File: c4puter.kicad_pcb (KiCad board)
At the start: 6 copper layers, 200 x 200 mm, 207 parts, among them J1 PDI, J2 MICROSD, J7 19V 3A, J8 DEBUG, Q1 AOD4189, Q2 AOD4189, Q3 2N7002, U1 ATXMEGA8E5-MU

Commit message: workworkwork
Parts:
- removed REF**: MP, MP
- added C57: 22u, IPC7351-Nominal:CAPC2012X70, F.Cu at (48.8, 161.5)
- added C59: C-0402, IPC7351-Nominal:CAPC1005X55, F.Cu at (48.8, 164.2)
- added C75: 22u, IPC7351-Nominal:CAPC2012X70, F.Cu at (57.5, 162.8)
- added C76: 22u, IPC7351-Nominal:CAPC2012X70, F.Cu at (55.2, 162.8)
- added L2: 2u2, manuf:BOURNS-SRN3015, F.Cu at (52.0, 157.8)
- added MP1: SCREW, mech:SCREW-4-SUPPORTED, F.Cu at (119.0, 104.0)
- added MP2: SCREW, mech:SCREW-4-SUPPORTED, F.Cu at (77.0, 130.0)
- added MP3: SCREW, mech:SCREW-4-SUPPORTED, F.Cu at (33.0, 104.0)
- added MP4: SCREW, mech:SCREW-4-SUPPORTED, F.Cu at (92.0, 32.0)
- added Q5: BSH203, smd-semi:SOT-23, F.Cu at (56.5, 159.0)
- added R57: R-0402, IPC7351-Nominal:RESC1005X40, F.Cu at (51.5, 165.8)
- added R61: R-0402, IPC7351-Nominal:RESC1005X40, F.Cu at (48.8, 165.8)
- added R62: 100, IPC7351-Nominal:RESC1608X50, F.Cu at (56.5, 156.2)
- added U2: AS7C38098A, IPC7351-Nominal:SOP80P1176X120-44, F.Cu at (61.0, 133.0)
- added U3: AS7C38098A, IPC7351-Nominal:SOP80P1176X120-44, F.Cu at (93.0, 133.0)
- added U5: AP3429A, smd-semi:SOT-23-5, F.Cu at (52.0, 162.5)
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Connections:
- net /PerBus/PCI_AD00 renamed /PCI/AD0
- net /PerBus/PCI_AD02 renamed /PCI/AD2
- net /PerBus/PCI_AD03 renamed /PCI/AD3
- net /PerBus/PCI_AD04 renamed /PCI/AD4
- net /PerBus/PCI_AD05 renamed /PCI/AD5
- net /PerBus/PCI_AD06 renamed /PCI/AD6
- net /PerBus/PCI_AD07 renamed /PCI/AD7
- net /PerBus/PCI_AD08 renamed /PCI/AD8
- net /PerBus/PCI_AD09 renamed /PCI/AD9
- net /PerBus/PCI_AD10 renamed /PCI/AD10
- net /PerBus/PCI_AD11 renamed /PCI/AD11
- net /PerBus/PCI_AD12 renamed /PCI/AD12
- net /PerBus/PCI_AD13 renamed /PCI/AD13
- net /PerBus/PCI_AD14 renamed /PCI/AD14
- net /PerBus/PCI_AD15 renamed /PCI/AD15
- net /PerBus/PCI_AD16 renamed /PCI/AD16
- net /PerBus/PCI_AD17 renamed /PCI/AD17
- net /PerBus/PCI_AD18 renamed /PCI/AD18
- net /PerBus/PCI_AD19 renamed /PCI/AD19
- net /PerBus/PCI_AD20 renamed /PCI/AD20
- net /PerBus/PCI_AD21 renamed /PCI/AD21
- net /PerBus/PCI_AD22 renamed /PCI/AD22
- net /PerBus/PCI_AD23 renamed /PCI/AD23
- net /PerBus/PCI_AD24 renamed /PCI/AD24
- net /PerBus/PCI_AD25 renamed /PCI/AD25
- net /PerBus/PCI_AD26 renamed /PCI/AD26
- net /PerBus/PCI_AD27 renamed /PCI/AD27
- net /PerBus/PCI_AD28 renamed /PCI/AD28
- net /PerBus/PCI_AD29 renamed /PCI/AD29
- net /PerBus/PCI_AD30 renamed /PCI/AD30
- net /PerBus/PCI_AD31 renamed /PCI/AD31
- net /PerBus/PCI_CBE#0 renamed /PCI/~CBE0
- net /PerBus/PCI_CBE#1 renamed /PCI/~CBE1
- net /PerBus/PCI_CBE#2 renamed /PCI/~CBE2
- net /PerBus/PCI_CBE#3 renamed /PCI/~CBE3
- net /PerBus/PCI_CLK renamed /PCI/CLK
- net /PerBus/PCI_DEVSEL# renamed /PCI/~DEVSEL
- net /PerBus/PCI_FRAME# renamed /PCI/~FRAME
- net /PerBus/PCI_GNT#0 renamed /PCI/~GNT0
- net /PerBus/PCI_GNT#1 renamed /PCI/~GNT1
- net /PerBus/PCI_GNT#2 renamed /PCI/~GNT2
- net /PerBus/PCI_GNT#3 renamed /PCI/~GNT3
- net /PerBus/PCI_IDSEL0 renamed /PCI/IDSEL0
- net /PerBus/PCI_IDSEL1 renamed /PCI/IDSEL1
- net /PerBus/PCI_IDSEL2 renamed /PCI/IDSEL2
- net /PerBus/PCI_IDSEL3 renamed /PCI/IDSEL3
- net /PerBus/PCI_INTA# renamed /PCI/~INT0
- net /PerBus/PCI_INTB# renamed /PCI/~INT1
- net /PerBus/PCI_INTC# renamed /PCI/~INT2
- net /PerBus/PCI_INTD# renamed /PCI/~INT3
- net /PerBus/PCI_IRDY# renamed /PCI/~IRDY
- net /PerBus/PCI_LOCK# renamed /PCI/~LOCK
- net /PerBus/PCI_M66EN renamed /PCI/M66EN
- net /PerBus/PCI_N12 renamed N12_PCI
- net /PerBus/PCI_P12 renamed P12_PCI
- net /PerBus/PCI_P5 renamed P5_PCI
- net /PerBus/PCI_PAR renamed /PCI/PAR
- net /PerBus/PCI_PERR# renamed /Multibridge/~PCI_PERR
- net /PerBus/PCI_PRSNT1#0 renamed /PCI/~PRSNT1_0
- net /PerBus/PCI_PRSNT1#1 renamed /PCI/~PRSNT1_1
- net /PerBus/PCI_PRSNT1#2 renamed /PCI/~PRSNT1_2
- net /PerBus/PCI_PRSNT1#3 renamed /PCI/~PRSNT1_3
- net /PerBus/PCI_PRSNT2#0 renamed /PCI/~PRSNT2_0
- net /PerBus/PCI_PRSNT2#1 renamed /PCI/~PRSNT2_1
- net /PerBus/PCI_PRSNT2#2 renamed /PCI/~PRSNT2_2
- net /PerBus/PCI_PRSNT2#3 renamed /PCI/~PRSNT2_3
- net /PerBus/PCI_REQ#0 renamed /Multibridge/~PCI_REQ0
- net /PerBus/PCI_REQ#1 renamed /Multibridge/~PCI_REQ1
- net /PerBus/PCI_REQ#2 renamed /Multibridge/~PCI_REQ2
- net /PerBus/PCI_REQ#3 renamed /Multibridge/~PCI_REQ3
- net /PerBus/PCI_RST# renamed /PCI/~RST
- net /PerBus/PCI_SERR# renamed /Multibridge/~PCI_SERR
- net /PerBus/PCI_SMBCLK renamed /PCI/SCL
- net /PerBus/PCI_SMBDAT renamed /PCI/SDA
- net /PerBus/PCI_STOP# renamed /Multibridge/~PCI_STOP
- net /PerBus/PCI_TCK renamed /PCI/PCI_TCK
- net /PerBus/PCI_TDI renamed /PCI/PCI_TDI
- net /PerBus/PCI_TDO renamed /PCI/PCI_TDO
- net /PerBus/PCI_TMS renamed /PCI/PCI_TMS
- net /PerBus/PCI_TRDY# renamed /Multibridge/~PCI_TRDY
- net /PerBus/PCI_TRST# renamed /PCI/PCI_TRST#
- net Net-(BRIDGE1-PadC12) renamed /Multibridge/SDRAMCLK
- net Net-(BRIDGE1-PadM20) renamed /Multibridge/PCICLK
- net VCCAUX renamed P3V3_BRIDGE
- net VCORE renamed P1V2_BRIDGE
- BRIDGE1 pad AB12: /PerBus/PCI_PME# -> Net-(BRIDGE1-PadAB12)
- BRIDGE1 pad T19: Net-(BRIDGE1-PadT19) -> /Multibridge/DQ63
- BRIDGE1 pad T20: /Multibridge/DQ63 -> Net-(BRIDGE1-PadT20)
- BRIDGE1 pad Y4: /PerBus/PCI_AD01 -> /PCI/AD1
- C37 pad 1: /PerBus/PCI_VIO -> P3V3_PCI
- C38 pad 1: /PerBus/PCI_P3V3 -> P3V3_PCI
- C41 pad 1: /PerBus/PCI_VIO -> P3V3_PCI
- C42 pad 1: /PerBus/PCI_P3V3 -> P3V3_PCI
- C45 pad 1: /PerBus/PCI_VIO -> P3V3_PCI
- C46 pad 1: /PerBus/PCI_P3V3 -> P3V3_PCI
- C49 pad 1: /PerBus/PCI_VIO -> P3V3_PCI
- C50 pad 1: /PerBus/PCI_P3V3 -> P3V3_PCI
- CPU0 pad A1: (no net) -> GND
- CPU0 pad A10: Net-(CPU0-PadA10) -> (no net)
- CPU0 pad A11: Net-(CPU0-PadA11) -> (no net)
- CPU0 pad A12: Net-(CPU0-PadA12) -> (no net)
- CPU0 pad A13: Net-(CPU0-PadA13) -> (no net)
- CPU0 pad A14: Net-(CPU0-PadA14) -> (no net)
- CPU0 pad A15: Net-(CPU0-PadA15) -> (no net)
- CPU0 pad A16: Net-(CPU0-PadA16) -> (no net)
- CPU0 pad A17: Net-(CPU0-PadA17) -> (no net)
- CPU0 pad A18: Net-(CPU0-PadA18) -> (no net)
- CPU0 pad A19: (no net) -> /Power Distrib/CPU0_TDO
- CPU0 pad A22: (no net) -> GND
- CPU0 pad A3: Net-(CPU0-PadA3) -> (no net)
- CPU0 pad A4: Net-(CPU0-PadA4) -> (no net)
- CPU0 pad A5: Net-(CPU0-PadA5) -> (no net)
- CPU0 pad A6: Net-(CPU0-PadA6) -> (no net)
- CPU0 pad A7: Net-(CPU0-PadA7) -> (no net)
- CPU0 pad A8: Net-(CPU0-PadA8) -> (no net)
- CPU0 pad A9: Net-(CPU0-PadA9) -> (no net)
- CPU0 pad AA1: (no net) -> Net-(CPU0-PadAA1)
- CPU0 pad AA10: (no net) -> Net-(CPU0-PadAA10)
- CPU0 pad AA11: (no net) -> P3V3_CPU
- CPU0 pad AA12: (no net) -> Net-(CPU0-PadAA12)
- CPU0 pad AA13: (no net) -> GND
- CPU0 pad AA14: (no net) -> Net-(CPU0-PadAA14)
- CPU0 pad AA15: (no net) -> P3V3_CPU
- CPU0 pad AA16: (no net) -> Net-(CPU0-PadAA16)
- CPU0 pad AA17: (no net) -> GND
- CPU0 pad AA18: (no net) -> Net-(CPU0-PadAA18)
- CPU0 pad AA19: (no net) -> P3V3_CPU
- CPU0 pad AA2: (no net) -> Net-(CPU0-PadAA2)
- CPU0 pad AA20: (no net) -> Net-(CPU0-PadAA20)
- CPU0 pad AA21: (no net) -> Net-(CPU0-PadAA21)
- CPU0 pad AA22: (no net) -> Net-(CPU0-PadAA22)
- CPU0 pad AA3: (no net) -> P3V3_CPU
- CPU0 pad AA4: (no net) -> Net-(CPU0-PadAA4)
- CPU0 pad AA5: (no net) -> GND
- CPU0 pad AA6: (no net) -> Net-(CPU0-PadAA6)
- CPU0 pad AA7: (no net) -> P3V3_CPU
- CPU0 pad AA8: (no net) -> Net-(CPU0-PadAA8)
- CPU0 pad AA9: (no net) -> GND
- CPU0 pad AB1: (no net) -> GND
- CPU0 pad AB10: (no net) -> Net-(CPU0-PadAB10)
- CPU0 pad AB11: (no net) -> Net-(CPU0-PadAB11)
- CPU0 pad AB12: (no net) -> Net-(CPU0-PadAB12)
- CPU0 pad AB13: (no net) -> Net-(CPU0-PadAB13)
- CPU0 pad AB14: (no net) -> Net-(CPU0-PadAB14)
- CPU0 pad AB15: (no net) -> Net-(CPU0-PadAB15)
- CPU0 pad AB16: (no net) -> Net-(CPU0-PadAB16)
- CPU0 pad AB17: (no net) -> Net-(CPU0-PadAB17)
- CPU0 pad AB18: (no net) -> Net-(CPU0-PadAB18)
- CPU0 pad AB19: (no net) -> Net-(CPU0-PadAB19)
- CPU0 pad AB2: (no net) -> Net-(CPU0-PadAB2)
- CPU0 pad AB20: (no net) -> Net-(CPU0-PadAB20)
- CPU0 pad AB21: (no net) -> Net-(CPU0-PadAB21)
- CPU0 pad AB22: (no net) -> GND
- CPU0 pad AB3: (no net) -> Net-(CPU0-PadAB3)
- CPU0 pad AB4: (no net) -> Net-(CPU0-PadAB4)
- CPU0 pad AB5: (no net) -> Net-(CPU0-PadAB5)
- CPU0 pad AB6: (no net) -> Net-(CPU0-PadAB6)
- CPU0 pad AB7: (no net) -> Net-(CPU0-PadAB7)
- CPU0 pad AB8: (no net) -> Net-(CPU0-PadAB8)
- CPU0 pad AB9: (no net) -> Net-(CPU0-PadAB9)
- CPU0 pad B10: Net-(CPU0-PadB10) -> (no net)
- CPU0 pad B11: Net-(CPU0-PadB11) -> (no net)
- CPU0 pad B12: Net-(CPU0-PadB12) -> (no net)
- CPU0 pad B13: (no net) -> GND
- CPU0 pad B14: Net-(CPU0-PadB14) -> (no net)
- CPU0 pad B15: Net-(CPU0-PadB15) -> (no net)
- CPU0 pad B16: Net-(CPU0-PadB16) -> (no net)
- CPU0 pad B17: (no net) -> GND
- CPU0 pad B18: Net-(CPU0-PadB18) -> (no net)
- CPU0 pad B19: Net-(CPU0-PadB19) -> (no net)
- CPU0 pad B4: Net-(CPU0-PadB4) -> (no net)
- CPU0 pad B5: (no net) -> GND
- CPU0 pad B6: Net-(CPU0-PadB6) -> (no net)
- CPU0 pad B7: Net-(CPU0-PadB7) -> (no net)
- CPU0 pad B8: Net-(CPU0-PadB8) -> (no net)
- CPU0 pad B9: (no net) -> GND
- CPU0 pad C10: Net-(CPU0-PadC10) -> (no net)
- CPU0 pad C11: Net-(CPU0-PadC11) -> (no net)
- CPU0 pad C12: Net-(CPU0-PadC12) -> (no net)
- CPU0 pad C13: Net-(CPU0-PadC13) -> (no net)
- CPU0 pad C14: Net-(CPU0-PadC14) -> (no net)
- CPU0 pad C15: Net-(CPU0-PadC15) -> (no net)
- CPU0 pad C16: Net-(CPU0-PadC16) -> (no net)
- CPU0 pad C17: Net-(CPU0-PadC17) -> (no net)
- CPU0 pad C18: (no net) -> /Power Distrib/CPU0_TMS
- CPU0 pad C5: Net-(CPU0-PadC5) -> (no net)
- CPU0 pad C6: Net-(CPU0-PadC6) -> (no net)
- CPU0 pad C7: Net-(CPU0-PadC7) -> (no net)
- CPU0 pad C8: Net-(CPU0-PadC8) -> (no net)
- CPU0 pad C9: Net-(CPU0-PadC9) -> (no net)
- CPU0 pad D10: Net-(CPU0-PadD10) -> (no net)
- CPU0 pad D11: Net-(CPU0-PadD11) -> (no net)
- CPU0 pad D12: Net-(CPU0-PadD12) -> (no net)
- CPU0 pad D13: Net-(CPU0-PadD13) -> (no net)
- CPU0 pad D14: Net-(CPU0-PadD14) -> (no net)
- CPU0 pad D15: Net-(CPU0-PadD15) -> (no net)
- CPU0 pad D16: (no net) -> P3V3_CPU
- CPU0 pad D17: Net-(CPU0-PadD17) -> (no net)
- CPU0 pad D18: (no net) -> GND
- CPU0 pad D4: (no net) -> GND
- CPU0 pad D6: Net-(CPU0-PadD6) -> (no net)
- CPU0 pad D7: Net-(CPU0-PadD7) -> (no net)
- CPU0 pad D8: Net-(CPU0-PadD8) -> (no net)
- CPU0 pad D9: Net-(CPU0-PadD9) -> (no net)
- CPU0 pad E11: (no net) -> GND
- CPU0 pad E12: Net-(CPU0-PadE12) -> (no net)
- CPU0 pad E13: Net-(CPU0-PadE13) -> (no net)
- CPU0 pad E14: Net-(CPU0-PadE14) -> (no net)
- CPU0 pad E15: (no net) -> GND
- CPU0 pad E16: Net-(CPU0-PadE16) -> (no net)
- CPU0 pad E17: Net-(CPU0-PadE17) -> (no net)
- CPU0 pad E18: (no net) -> /Power Distrib/CPU0_TDI
- CPU0 pad E2: (no net) -> GND
- CPU0 pad E21: (no net) -> GND
- CPU0 pad E7: (no net) -> GND
- CPU0 pad E9: Net-(CPU0-PadE9) -> (no net)
- CPU0 pad F11: (no net) -> P3V3_CPU
- CPU0 pad F12: Net-(CPU0-PadF12) -> (no net)
- CPU0 pad F13: Net-(CPU0-PadF13) -> (no net)
- CPU0 pad F14: Net-(CPU0-PadF14) -> (no net)
- CPU0 pad F15: Net-(CPU0-PadF15) -> (no net)
- CPU0 pad G10: Net-(CPU0-PadG10) -> (no net)
- CPU0 pad G12: (no net) -> P3V3_CPU
- CPU0 pad G13: Net-(CPU0-PadG13) -> (no net)
- CPU0 pad G14: Net-(CPU0-PadG14) -> (no net)
- CPU0 pad G15: (no net) -> /Power Distrib/CPU0_TCK
- CPU0 pad G18: (no net) -> GND
- CPU0 pad G5: (no net) -> GND
- CPU0 pad H12: Net-(CPU0-PadH12) -> (no net)
- CPU0 pad H13: Net-(CPU0-PadH13) -> (no net)
- CPU0 pad H14: Net-(CPU0-PadH14) -> (no net)
- CPU0 pad H15: (no net) -> P3V3_CPU
- CPU0 pad H7: (no net) -> GND
- CPU0 pad H9: (no net) -> P3V3_CPU
- CPU0 pad J10: (no net) -> P1V2_CPU
- CPU0 pad J11: (no net) -> GND
- CPU0 pad J12: (no net) -> P1V2_CPU
- CPU0 pad J13: (no net) -> GND
- CPU0 pad J14: (no net) -> P1V2_CPU
- CPU0 pad J15: (no net) -> GND
- CPU0 pad J2: (no net) -> GND
- CPU0 pad J21: (no net) -> GND
- CPU0 pad J8: (no net) -> P1V2_CPU
- CPU0 pad J9: (no net) -> GND
- CPU0 pad K10: (no net) -> GND
- CPU0 pad K11: (no net) -> P1V2_CPU
- CPU0 pad K12: (no net) -> GND
- CPU0 pad K13: (no net) -> P1V2_CPU
- CPU0 pad K14: (no net) -> GND
- CPU0 pad K15: (no net) -> P3V3_CPU
- CPU0 pad K9: (no net) -> P1V2_CPU
- CPU0 pad L10: (no net) -> P1V2_CPU
- CPU0 pad L11: (no net) -> GND
- CPU0 pad L12: (no net) -> P1V2_CPU
- CPU0 pad L13: (no net) -> GND
- CPU0 pad L14: (no net) -> P1V2_CPU
- CPU0 pad L18: (no net) -> GND
- CPU0 pad L5: (no net) -> GND
- CPU0 pad L8: (no net) -> P3V3_CPU
- CPU0 pad L9: (no net) -> GND
- CPU0 pad M10: (no net) -> GND
- CPU0 pad M11: (no net) -> P1V2_CPU
- CPU0 pad M12: (no net) -> GND
- CPU0 pad M13: (no net) -> P1V2_CPU
- CPU0 pad M14: (no net) -> GND
- CPU0 pad M15: (no net) -> P3V3_CPU
- CPU0 pad M9: (no net) -> P1V2_CPU
- CPU0 pad N10: (no net) -> P1V2_CPU
- CPU0 pad N11: (no net) -> GND
- CPU0 pad N12: (no net) -> P1V2_CPU
- CPU0 pad N13: (no net) -> GND
- CPU0 pad N14: (no net) -> P1V2_CPU
- CPU0 pad N15: (no net) -> /Power Distrib/CPU0_SUSP
- CPU0 pad N17: (no net) -> GND
- CPU0 pad N2: (no net) -> GND
- CPU0 pad N21: (no net) -> GND
- CPU0 pad N8: (no net) -> P3V3_CPU
- CPU0 pad N9: (no net) -> GND
- CPU0 pad P10: (no net) -> GND
- CPU0 pad P11: (no net) -> P1V2_CPU
- CPU0 pad P12: (no net) -> GND
- CPU0 pad P13: (no net) -> P1V2_CPU
- CPU0 pad P14: (no net) -> GND
- CPU0 pad P9: (no net) -> P1V2_CPU
- CPU0 pad R10: (no net) -> P3V3_CPU
- CPU0 pad R11: (no net) -> Net-(CPU0-PadR11)
- CPU0 pad R12: (no net) -> P3V3_CPU
- CPU0 pad R14: (no net) -> P1V2_CPU
- CPU0 pad R18: (no net) -> GND
- CPU0 pad R5: (no net) -> GND
- CPU0 pad R6: (no net) -> P3V3_CPU
- CPU0 pad R7: (no net) -> Net-(CPU0-PadR7)
- CPU0 pad R8: (no net) -> Net-(CPU0-PadR8)
- CPU0 pad R9: (no net) -> Net-(CPU0-PadR9)
- CPU0 pad T11: (no net) -> Net-(CPU0-PadT11)
- CPU0 pad T13: (no net) -> P3V3_CPU
- CPU0 pad T5: (no net) -> Net-(CPU0-PadT5)
- CPU0 pad T6: (no net) -> Net-(CPU0-PadT6)
- CPU0 pad T7: (no net) -> Net-(CPU0-PadT7)
- CPU0 pad T9: (no net) -> P3V3_CPU
- CPU0 pad U11: (no net) -> P3V3_CPU
- CPU0 pad U13: (no net) -> Net-(CPU0-PadU13)
- CPU0 pad U14: (no net) -> Net-(CPU0-PadU14)
- CPU0 pad U15: (no net) -> Net-(CPU0-PadU15)
- CPU0 pad U2: (no net) -> GND
- CPU0 pad U21: (no net) -> GND
- CPU0 pad U6: (no net) -> Net-(CPU0-PadU6)
- CPU0 pad U7: (no net) -> GND
- CPU0 pad U9: (no net) -> Net-(CPU0-PadU9)
- CPU0 pad V10: (no net) -> GND
- CPU0 pad V11: (no net) -> Net-(CPU0-PadV11)
- CPU0 pad V12: (no net) -> P3V3_CPU
- CPU0 pad V13: (no net) -> Net-(CPU0-PadV13)
- CPU0 pad V14: (no net) -> GND
- CPU0 pad V15: (no net) -> Net-(CPU0-PadV15)
- CPU0 pad V16: (no net) -> P3V3_CPU
- CPU0 pad V4: (no net) -> GND
- CPU0 pad V5: (no net) -> Net-(CPU0-PadV5)
- CPU0 pad V6: (no net) -> P3V3_CPU
- CPU0 pad V7: (no net) -> Net-(CPU0-PadV7)
- CPU0 pad V8: (no net) -> P3V3_CPU
- CPU0 pad V9: (no net) -> Net-(CPU0-PadV9)
- CPU0 pad W10: (no net) -> Net-(CPU0-PadW10)
- CPU0 pad W11: (no net) -> Net-(CPU0-PadW11)
- CPU0 pad W12: (no net) -> Net-(CPU0-PadW12)
- CPU0 pad W13: (no net) -> Net-(CPU0-PadW13)
- CPU0 pad W14: (no net) -> Net-(CPU0-PadW14)
- CPU0 pad W15: (no net) -> Net-(CPU0-PadW15)
- CPU0 pad W16: (no net) -> GND
- CPU0 pad W18: (no net) -> Net-(CPU0-PadW18)
- CPU0 pad W19: (no net) -> GND
- CPU0 pad W4: (no net) -> Net-(CPU0-PadW4)
- CPU0 pad W5: (no net) -> P3V3_CPU
- CPU0 pad W6: (no net) -> Net-(CPU0-PadW6)
- CPU0 pad W7: (no net) -> GND
- CPU0 pad W8: (no net) -> Net-(CPU0-PadW8)
- CPU0 pad W9: (no net) -> Net-(CPU0-PadW9)
- CPU0 pad Y10: (no net) -> Net-(CPU0-PadY10)
- CPU0 pad Y11: (no net) -> Net-(CPU0-PadY11)
- CPU0 pad Y12: (no net) -> Net-(CPU0-PadY12)
- CPU0 pad Y13: (no net) -> Net-(CPU0-PadY13)
- CPU0 pad Y14: (no net) -> Net-(CPU0-PadY14)
- CPU0 pad Y15: (no net) -> Net-(CPU0-PadY15)
- CPU0 pad Y16: (no net) -> Net-(CPU0-PadY16)
- CPU0 pad Y17: (no net) -> Net-(CPU0-PadY17)
- CPU0 pad Y18: (no net) -> Net-(CPU0-PadY18)
- CPU0 pad Y19: (no net) -> Net-(CPU0-PadY19)
- CPU0 pad Y20: (no net) -> Net-(CPU0-PadY20)
- CPU0 pad Y21: (no net) -> Net-(CPU0-PadY21)
- CPU0 pad Y22: (no net) -> Net-(CPU0-PadY22)
- CPU0 pad Y3: (no net) -> Net-(CPU0-PadY3)
- CPU0 pad Y4: (no net) -> Net-(CPU0-PadY4)
- CPU0 pad Y5: (no net) -> Net-(CPU0-PadY5)
- CPU0 pad Y6: (no net) -> Net-(CPU0-PadY6)
- CPU0 pad Y7: (no net) -> Net-(CPU0-PadY7)
- CPU0 pad Y8: (no net) -> Net-(CPU0-PadY8)
- CPU0 pad Y9: (no net) -> Net-(CPU0-PadY9)
- CPU1 pad A1: (no net) -> GND
- CPU1 pad A19: (no net) -> /Power Distrib/CPU1_TDO
- CPU1 pad A22: (no net) -> GND
- CPU1 pad AA13: (no net) -> GND
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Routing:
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- added copper zone on B.Cu, net P3V3_PCI
- removed copper zone on B.Cu, net /PerBus/PCI_P3V3
- removed copper zone on B.Cu, net /PerBus/PCI_VIO
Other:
- net class Default: clearance 0.125 -> 0.1016; trace_width 0.125 -> 0.1016
- rule trace_clearance: 0.125 -> 0.1016

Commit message: workworkworkwork
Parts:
- removed C57, C75, C76: 22u, IPC7351-Nominal:CAPC2012X70
- removed C59: C-0402, IPC7351-Nominal:CAPC1005X55
- removed L2: 2u2, manuf:BOURNS-SRN3015
- removed Q5: BSH203, smd-semi:SOT-23
- removed R57, R61: R-0402, IPC7351-Nominal:RESC1005X40
- removed R62: 100, IPC7351-Nominal:RESC1608X50
- removed U5: AP3429A, smd-semi:SOT-23-5

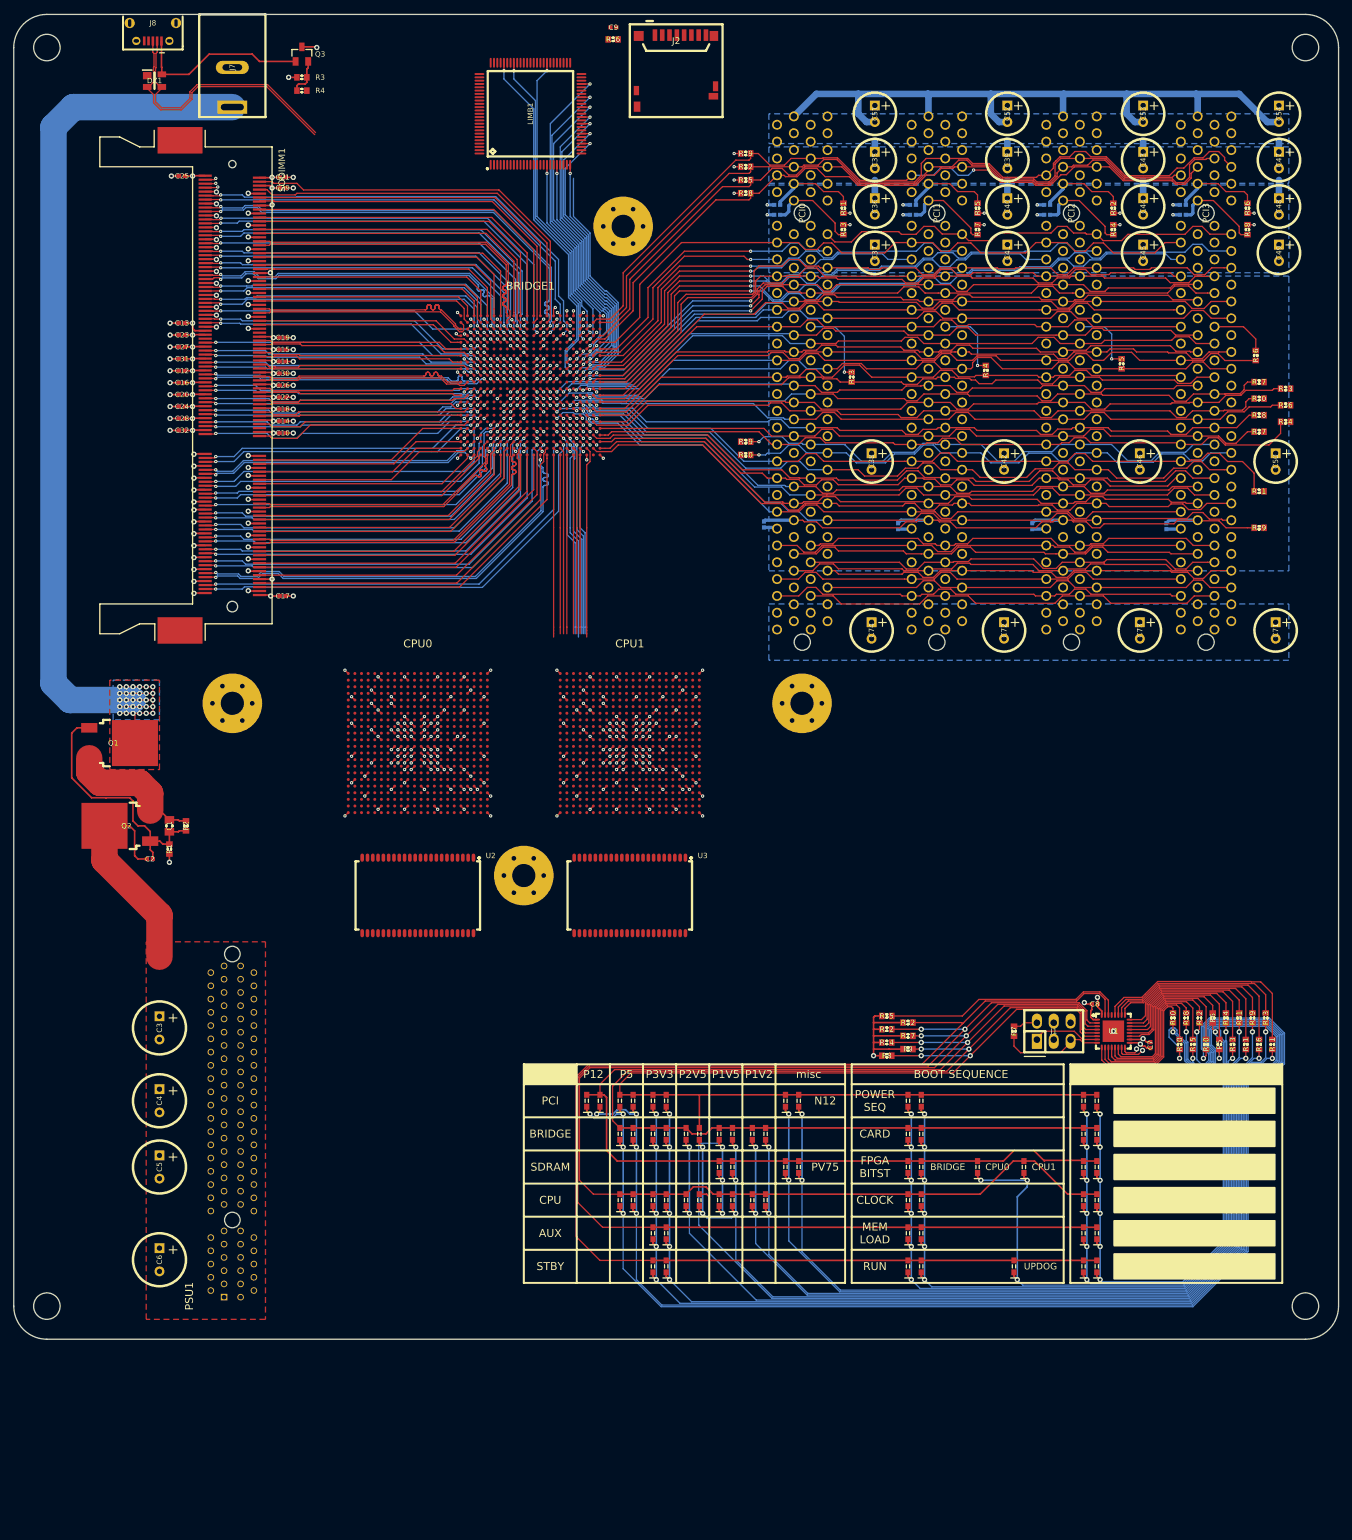
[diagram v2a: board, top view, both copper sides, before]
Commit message: Route CPU bus and cache
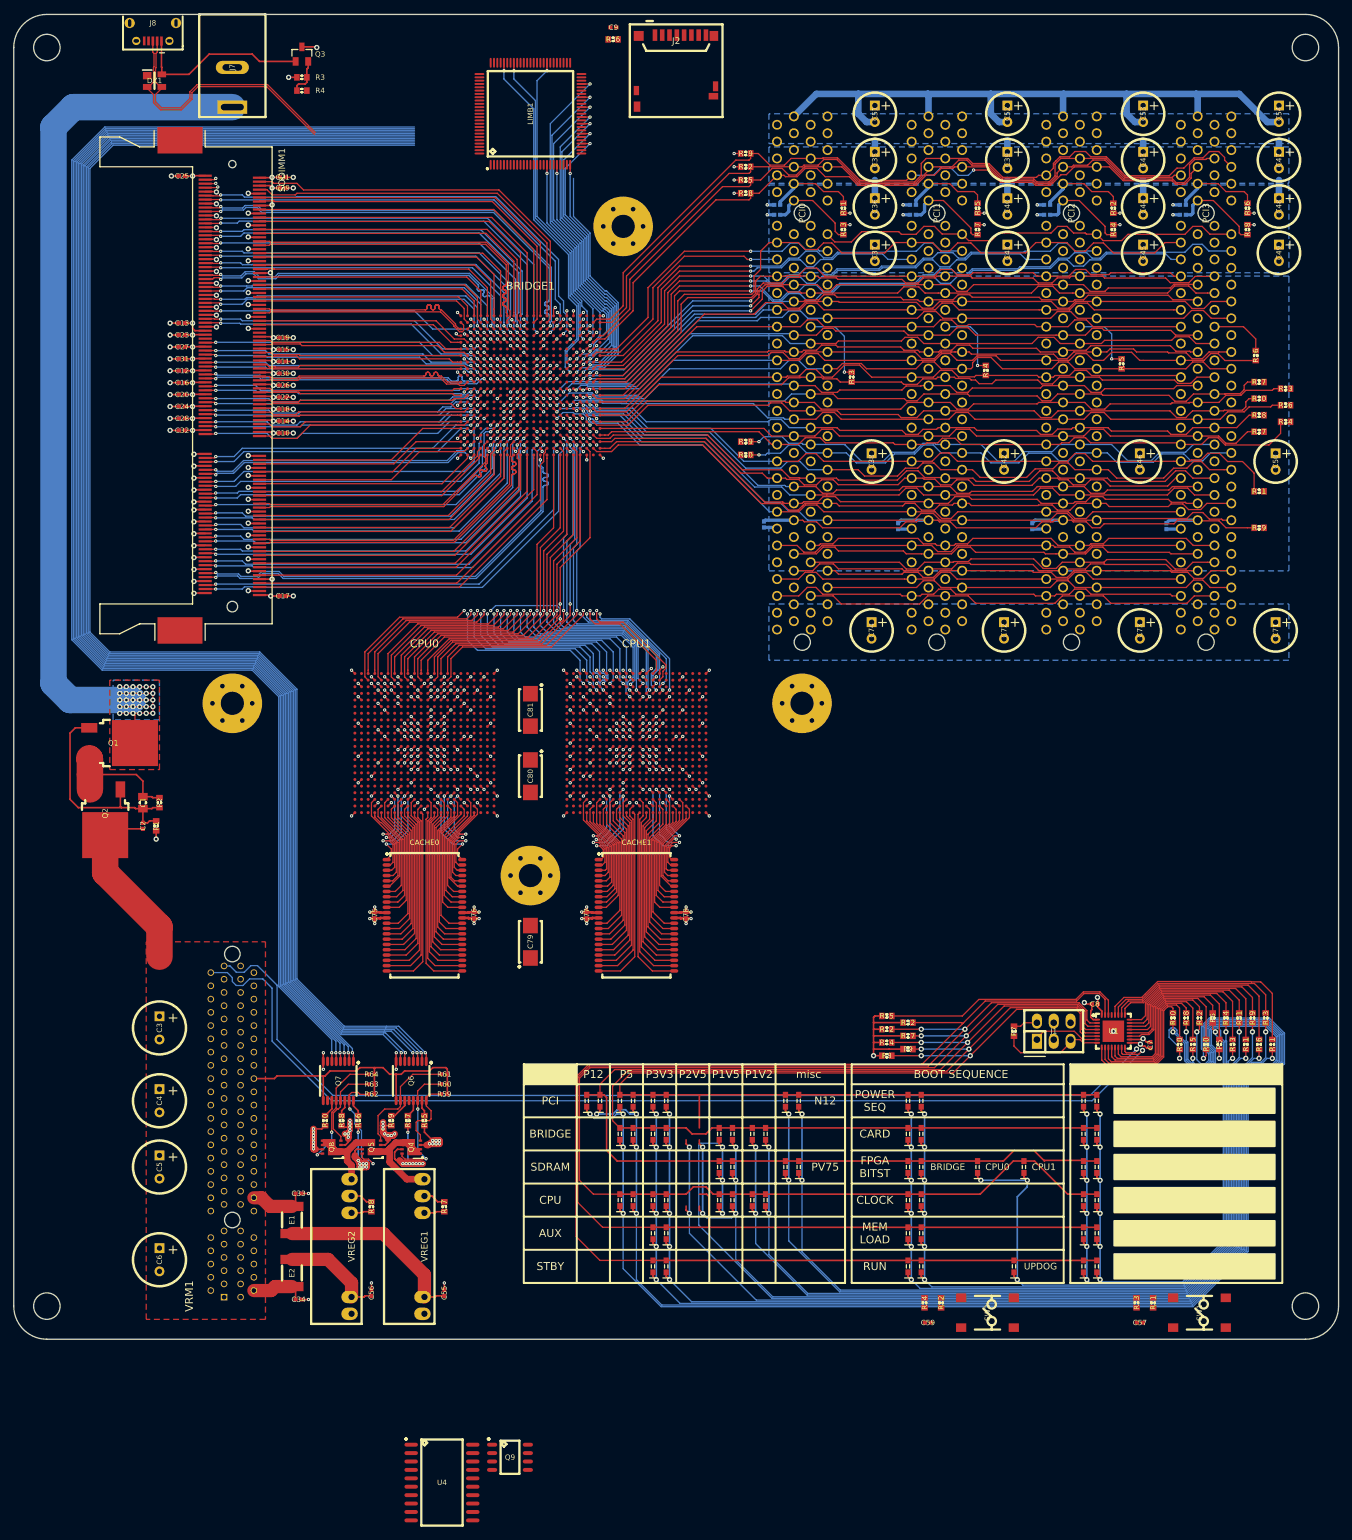
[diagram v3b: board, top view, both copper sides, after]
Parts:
- removed DS19: BRG_P2V5(R), smd-semi:LED-0603
- removed DS20: CPU_P2V5(R), smd-semi:LED-0603
- removed DS21: BRG_P2V5(G), smd-semi:LED-0603
- removed DS22: CPU_P2V5(G), smd-semi:LED-0603
- added C33: 100n, IPC7351-Nominal:CAPC1005X55, F.Cu at (43.0, 178.0)
- added C34: 100n, IPC7351-Nominal:CAPC1005X55, F.Cu at (43.0, 194.0)
- added C55: 100n, IPC7351-Nominal:CAPC1005X55, F.Cu at (65.0, 193.0)
- added C56: 100n, IPC7351-Nominal:CAPC1005X55, F.Cu at (54.0, 193.0)
- added C57: 100n, IPC7351-Nominal:CAPC1005X55, F.Cu at (170.0, 197.5)
- added C59: 100n, IPC7351-Nominal:CAPC1005X55, F.Cu at (138.0, 197.5)
- added C75: 1u, IPC7351-Nominal:CAPC1005X55, F.Cu at (54.5, 136.0)
- added C76: 1u, IPC7351-Nominal:CAPC1005X55, F.Cu at (69.5, 136.0)
- added C77: 1u, IPC7351-Nominal:CAPC1005X55, F.Cu at (86.5, 136.0)
- added C78: 1u, IPC7351-Nominal:CAPC1005X55, F.Cu at (101.5, 136.0)
- added C79: 330u/6v3, IPC7351-Nominal:CAPMP6032X280, F.Cu at (78.0, 140.0)
- added C80: 330u/6v3, IPC7351-Nominal:CAPMP6032X280, F.Cu at (78.0, 115.0)
- added C81: 330u/6v3, IPC7351-Nominal:CAPMP6032X280, F.Cu at (78.0, 105.0)
- added E1: 100, IPC7351-Nominal:CAPC4532X220, F.Cu at (42.0, 182.0)
- added E2: 100, IPC7351-Nominal:CAPC4532X220, F.Cu at (42.0, 190.0)
- added Q4: DMN3016LDN, manuf:DIODES-V-DFN3030-8, F.Cu at (60.0, 171.0)
- added Q5: DMN3016LDN, manuf:DIODES-V-DFN3030-8, F.Cu at (54.0, 171.0)
- added Q6: ULN2003APWR, IPC7351-Nominal:SOP65P640X120-16, F.Cu at (60.0, 161.0)
- added Q7: ULN2003APWR, IPC7351-Nominal:SOP65P640X120-16, F.Cu at (49.0, 161.0)
- added Q8: DMN3016LDN, manuf:DIODES-V-DFN3030-8, F.Cu at (48.0, 171.0)
- added Q9: DMN3018SSS, IPC7351-Nominal:SOIC127P600X175-8, F.Cu at (74.9, 217.8)
- added R57: 22k6, IPC7351-Nominal:RESC1608X50, F.Cu at (65.0, 180.0)
- added R58: 22k6, IPC7351-Nominal:RESC1608X50, F.Cu at (54.0, 180.0)
- added R59: 330k, IPC7351-Nominal:RESC1005X40, F.Cu at (65.0, 163.0)
- added R60: 330k, IPC7351-Nominal:RESC1005X40, F.Cu at (65.0, 161.5)
- added R61: 330k, IPC7351-Nominal:RESC1005X40, F.Cu at (65.0, 160.0)
- added R62: 330k, IPC7351-Nominal:RESC1005X40, F.Cu at (54.0, 163.0)
- added R63: 330k, IPC7351-Nominal:RESC1005X40, F.Cu at (54.0, 161.5)
- added R64: 330k, IPC7351-Nominal:RESC1005X40, F.Cu at (54.0, 160.0)
- added R65: 100, IPC7351-Nominal:RESC1608X50, F.Cu at (62.0, 167.0)
- added R66: 100, IPC7351-Nominal:RESC1608X50, F.Cu at (52.0, 167.0)
- added R67: 100, IPC7351-Nominal:RESC1608X50, F.Cu at (59.5, 167.0)
- added R68: 100, IPC7351-Nominal:RESC1608X50, F.Cu at (49.5, 167.0)
- added R69: 100, IPC7351-Nominal:RESC1608X50, F.Cu at (57.0, 167.0)
- added R70: 100, IPC7351-Nominal:RESC1608X50, F.Cu at (47.0, 167.0)
- added R71: 100k, IPC7351-Nominal:RESC1608X50, F.Cu at (172.0, 194.5)
- added R72: 100k, IPC7351-Nominal:RESC1608X50, F.Cu at (140.0, 194.5)
- added R73: 100k, IPC7351-Nominal:RESC1608X50, F.Cu at (169.5, 194.5)
- added R74: 100k, IPC7351-Nominal:RESC1608X50, F.Cu at (137.5, 194.5)
- added SW1: POWER, manuf:CK-PTS645-SMD, F.Cu at (179.0, 196.0)
- added SW2: SW, manuf:CK-PTS645-SMD, F.Cu at (147.0, 196.0)
- added U4: TPIC6B595DW, IPC7351-Nominal:SOIC127P1030X265-20, F.Cu at (64.6, 221.6)
- added VREG1: OKX-T/5-W5N-C, manuf:MURATA-OKX-T5-W5, F.Cu at (62.0, 186.0)
- added VREG2: OKX-T/5-W5N-C, manuf:MURATA-OKX-T5-W5, F.Cu at (51.0, 186.0)
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- renumbered U2 to CACHE0, U3 to CACHE1, PSU1 to VRM1
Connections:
- net /Multibridge/PCICLK renamed Net-(BRIDGE1-PadM20)
- net /Power/INT# renamed /Power/~INT
- BRIDGE1 pad AB12: Net-(BRIDGE1-PadAB12) -> /PCI/CLK
- BRIDGE1 pad AB18: /PCI/CLK -> Net-(BRIDGE1-PadAB18)
- BRIDGE1 pad C17: Net-(BRIDGE1-PadC17) -> /Multibridge/CPU_D0
- BRIDGE1 pad D9: Net-(BRIDGE1-PadD9) -> /Multibridge/CPU_D2
- BRIDGE1 pad E14: Net-(BRIDGE1-PadE14) -> /Multibridge/CPU_D1
- BRIDGE1 pad F12: Net-(BRIDGE1-PadF12) -> /Multibridge/CPU_D4
- BRIDGE1 pad F18: Net-(BRIDGE1-PadF18) -> /Multibridge/CPU_D15
- BRIDGE1 pad G13: Net-(BRIDGE1-PadG13) -> /Multibridge/CPU_D3
- BRIDGE1 pad G20: Net-(BRIDGE1-PadG20) -> /Multibridge/CPU_D19
- BRIDGE1 pad H13: Net-(BRIDGE1-PadH13) -> /Multibridge/CPU_D7
- BRIDGE1 pad H18: Net-(BRIDGE1-PadH18) -> /Multibridge/CPU_D16
- BRIDGE1 pad H5: Net-(BRIDGE1-PadH5) -> /Multibridge/CPU_D5
- BRIDGE1 pad J17: Net-(BRIDGE1-PadJ17) -> /Multibridge/CPU_D20
- BRIDGE1 pad J6: Net-(BRIDGE1-PadJ6) -> /Multibridge/CPU_D8
- BRIDGE1 pad J7: Net-(BRIDGE1-PadJ7) -> /Multibridge/CPU_D9
- BRIDGE1 pad K17: Net-(BRIDGE1-PadK17) -> /Multibridge/CPU_D31
- BRIDGE1 pad K18: Net-(BRIDGE1-PadK18) -> /Multibridge/CPU_D17
- BRIDGE1 pad K5: Net-(BRIDGE1-PadK5) -> /CPU0/BUSCLK
- BRIDGE1 pad K6: Net-(BRIDGE1-PadK6) -> /Multibridge/CPU_D10
- BRIDGE1 pad M5: Net-(BRIDGE1-PadM5) -> /Multibridge/CPU_D12
- BRIDGE1 pad N20: Net-(BRIDGE1-PadN20) -> /Multibridge/CPU_D11
- BRIDGE1 pad R1: Net-(BRIDGE1-PadR1) -> /Multibridge/CPU_D18
- BRIDGE1 pad R22: Net-(BRIDGE1-PadR22) -> /CPU0/ADDR#
- BRIDGE1 pad T1: Net-(BRIDGE1-PadT1) -> /Multibridge/CPU_WAIT#
- BRIDGE1 pad T2: Net-(BRIDGE1-PadT2) -> /Multibridge/CPU_D21
- BRIDGE1 pad T20: Net-(BRIDGE1-PadT20) -> /Multibridge/CPU_D14
- BRIDGE1 pad T21: Net-(BRIDGE1-PadT21) -> /Multibridge/CPU_D6
- BRIDGE1 pad T22: Net-(BRIDGE1-PadT22) -> /CPU0/BUSINT#
- BRIDGE1 pad T4: Net-(BRIDGE1-PadT4) -> /Multibridge/CPU_D28
- BRIDGE1 pad U1: Net-(BRIDGE1-PadU1) -> /Multibridge/CPU_D24
- BRIDGE1 pad U20: Net-(BRIDGE1-PadU20) -> /Multibridge/CPU_D13
- BRIDGE1 pad U22: Net-(BRIDGE1-PadU22) -> /Multibridge/CPU_WR#
- BRIDGE1 pad U3: Net-(BRIDGE1-PadU3) -> /Multibridge/CPU_D26
- BRIDGE1 pad U4: Net-(BRIDGE1-PadU4) -> /CPU0/BUSACK#
- BRIDGE1 pad V1: Net-(BRIDGE1-PadV1) -> /Multibridge/CPU_D22
- BRIDGE1 pad V2: Net-(BRIDGE1-PadV2) -> /Multibridge/CPU_D23
- BRIDGE1 pad V21: Net-(BRIDGE1-PadV21) -> /CPU1/BUSACK#
- BRIDGE1 pad V22: Net-(BRIDGE1-PadV22) -> /CPU0/BUSREQ#
- BRIDGE1 pad V3: Net-(BRIDGE1-PadV3) -> /Multibridge/CPU_D27
- BRIDGE1 pad W1: Net-(BRIDGE1-PadW1) -> /Multibridge/CPU_D25
- BRIDGE1 pad W20: Net-(BRIDGE1-PadW20) -> /CPU1/BUSINT#
- BRIDGE1 pad W22: Net-(BRIDGE1-PadW22) -> /CPU1/BUSREQ#
- BRIDGE1 pad W3: Net-(BRIDGE1-PadW3) -> /Multibridge/CPU_D30
- BRIDGE1 pad Y2: Net-(BRIDGE1-PadY2) -> /Multibridge/CPU_D29
- CACHE0 pad 1: Net-(U2-Pad1) -> /CPU0/CACHE_A4
- CACHE0 pad 10: Net-(U2-Pad10) -> /CPU0/CACHE_DQ3
- CACHE0 pad 11: Net-(U2-Pad11) -> P3V3_CPU
- CACHE0 pad 12: Net-(U2-Pad12) -> GND
- CACHE0 pad 13: Net-(U2-Pad13) -> /CPU0/CACHE_DQ4
- CACHE0 pad 14: Net-(U2-Pad14) -> /CPU0/CACHE_DQ5
- CACHE0 pad 15: Net-(U2-Pad15) -> /CPU0/CACHE_DQ6
- CACHE0 pad 16: Net-(U2-Pad16) -> /CPU0/CACHE_DQ7
- CACHE0 pad 17: Net-(U2-Pad17) -> /CPU0/CACHE_~WE
- CACHE0 pad 18: Net-(U2-Pad18) -> /CPU0/CACHE_A18
- CACHE0 pad 19: Net-(U2-Pad19) -> /CPU0/CACHE_A17
- CACHE0 pad 2: Net-(U2-Pad2) -> /CPU0/CACHE_A3
- CACHE0 pad 20: Net-(U2-Pad20) -> /CPU0/CACHE_A16
- CACHE0 pad 21: Net-(U2-Pad21) -> /CPU0/CACHE_A15
- CACHE0 pad 22: Net-(U2-Pad22) -> /CPU0/CACHE_A14
- CACHE0 pad 23: Net-(U2-Pad23) -> /CPU0/CACHE_A13
- CACHE0 pad 24: Net-(U2-Pad24) -> /CPU0/CACHE_A12
- CACHE0 pad 25: Net-(U2-Pad25) -> /CPU0/CACHE_A11
- CACHE0 pad 26: Net-(U2-Pad26) -> /CPU0/CACHE_A10
- CACHE0 pad 27: Net-(U2-Pad27) -> /CPU0/CACHE_A9
- CACHE0 pad 28: Net-(U2-Pad28) -> /CPU0/CACHE_A8
- CACHE0 pad 29: Net-(U2-Pad29) -> /CPU0/CACHE_DQ8
- CACHE0 pad 3: Net-(U2-Pad3) -> /CPU0/CACHE_A2
- CACHE0 pad 30: Net-(U2-Pad30) -> /CPU0/CACHE_DQ9
- CACHE0 pad 31: Net-(U2-Pad31) -> /CPU0/CACHE_DQ10
- CACHE0 pad 32: Net-(U2-Pad32) -> /CPU0/CACHE_DQ11
- CACHE0 pad 33: Net-(U2-Pad33) -> P3V3_CPU
- CACHE0 pad 34: Net-(U2-Pad34) -> GND
- CACHE0 pad 35: Net-(U2-Pad35) -> /CPU0/CACHE_DQ12
- CACHE0 pad 36: Net-(U2-Pad36) -> /CPU0/CACHE_DQ13
- CACHE0 pad 37: Net-(U2-Pad37) -> /CPU0/CACHE_DQ14
- CACHE0 pad 38: Net-(U2-Pad38) -> /CPU0/CACHE_DQ15
- CACHE0 pad 39: Net-(U2-Pad39) -> /CPU0/CACHE_~LB
- CACHE0 pad 4: Net-(U2-Pad4) -> /CPU0/CACHE_A1
- CACHE0 pad 40: Net-(U2-Pad40) -> /CPU0/CACHE_~UB
- CACHE0 pad 41: Net-(U2-Pad41) -> /CPU0/CACHE_~OE
- CACHE0 pad 42: Net-(U2-Pad42) -> /CPU0/CACHE_A7
- CACHE0 pad 43: Net-(U2-Pad43) -> /CPU0/CACHE_A6
- CACHE0 pad 44: Net-(U2-Pad44) -> /CPU0/CACHE_A5
- CACHE0 pad 5: Net-(U2-Pad5) -> /CPU0/CACHE_A0
- CACHE0 pad 6: Net-(U2-Pad6) -> /CPU0/CACHE_~CE
- CACHE0 pad 7: Net-(U2-Pad7) -> /CPU0/CACHE_DQ0
- CACHE0 pad 8: Net-(U2-Pad8) -> /CPU0/CACHE_DQ1
- CACHE0 pad 9: Net-(U2-Pad9) -> /CPU0/CACHE_DQ2
- CACHE1 pad 1: Net-(U3-Pad1) -> /CPU1/CACHE_A4
- CACHE1 pad 10: Net-(U3-Pad10) -> /CPU1/CACHE_DQ3
- CACHE1 pad 11: Net-(U3-Pad11) -> P3V3_CPU
- CACHE1 pad 12: Net-(U3-Pad12) -> GND
- CACHE1 pad 13: Net-(U3-Pad13) -> /CPU1/CACHE_DQ4
- CACHE1 pad 14: Net-(U3-Pad14) -> /CPU1/CACHE_DQ5
- CACHE1 pad 15: Net-(U3-Pad15) -> /CPU1/CACHE_DQ6
- CACHE1 pad 16: Net-(U3-Pad16) -> /CPU1/CACHE_DQ7
- CACHE1 pad 17: Net-(U3-Pad17) -> /CPU1/CACHE_~WE
- CACHE1 pad 18: Net-(U3-Pad18) -> /CPU1/CACHE_A18
- CACHE1 pad 19: Net-(U3-Pad19) -> /CPU1/CACHE_A17
- CACHE1 pad 2: Net-(U3-Pad2) -> /CPU1/CACHE_A3
- CACHE1 pad 20: Net-(U3-Pad20) -> /CPU1/CACHE_A16
- CACHE1 pad 21: Net-(U3-Pad21) -> /CPU1/CACHE_A15
- CACHE1 pad 22: Net-(U3-Pad22) -> /CPU1/CACHE_A14
- CACHE1 pad 23: Net-(U3-Pad23) -> /CPU1/CACHE_A13
- CACHE1 pad 24: Net-(U3-Pad24) -> /CPU1/CACHE_A12
- CACHE1 pad 25: Net-(U3-Pad25) -> /CPU1/CACHE_A11
- CACHE1 pad 26: Net-(U3-Pad26) -> /CPU1/CACHE_A10
- CACHE1 pad 27: Net-(U3-Pad27) -> /CPU1/CACHE_A9
- CACHE1 pad 28: Net-(U3-Pad28) -> /CPU1/CACHE_A8
- CACHE1 pad 29: Net-(U3-Pad29) -> /CPU1/CACHE_DQ8
- CACHE1 pad 3: Net-(U3-Pad3) -> /CPU1/CACHE_A2
- CACHE1 pad 30: Net-(U3-Pad30) -> /CPU1/CACHE_DQ9
- CACHE1 pad 31: Net-(U3-Pad31) -> /CPU1/CACHE_DQ10
- CACHE1 pad 32: Net-(U3-Pad32) -> /CPU1/CACHE_DQ11
- CACHE1 pad 33: Net-(U3-Pad33) -> P3V3_CPU
- CACHE1 pad 34: Net-(U3-Pad34) -> GND
- CACHE1 pad 35: Net-(U3-Pad35) -> /CPU1/CACHE_DQ12
- CACHE1 pad 36: Net-(U3-Pad36) -> /CPU1/CACHE_DQ13
- CACHE1 pad 37: Net-(U3-Pad37) -> /CPU1/CACHE_DQ14
- CACHE1 pad 38: Net-(U3-Pad38) -> /CPU1/CACHE_DQ15
- CACHE1 pad 39: Net-(U3-Pad39) -> /CPU1/CACHE_~LB
- CACHE1 pad 4: Net-(U3-Pad4) -> /CPU1/CACHE_A1
- CACHE1 pad 40: Net-(U3-Pad40) -> /CPU1/CACHE_~UB
- CACHE1 pad 41: Net-(U3-Pad41) -> /CPU1/CACHE_~OE
- CACHE1 pad 42: Net-(U3-Pad42) -> /CPU1/CACHE_A7
- CACHE1 pad 43: Net-(U3-Pad43) -> /CPU1/CACHE_A6
- CACHE1 pad 44: Net-(U3-Pad44) -> /CPU1/CACHE_A5
- CACHE1 pad 5: Net-(U3-Pad5) -> /CPU1/CACHE_A0
- CACHE1 pad 6: Net-(U3-Pad6) -> /CPU1/CACHE_~CE
- CACHE1 pad 7: Net-(U3-Pad7) -> /CPU1/CACHE_DQ0
- CACHE1 pad 8: Net-(U3-Pad8) -> /CPU1/CACHE_DQ1
- CACHE1 pad 9: Net-(U3-Pad9) -> /CPU1/CACHE_DQ2
- CPU0 pad A10: (no net) -> Net-(CPU0-PadA10)
- CPU0 pad A11: (no net) -> Net-(CPU0-PadA11)
- CPU0 pad A12: (no net) -> Net-(CPU0-PadA12)
- CPU0 pad A13: (no net) -> Net-(CPU0-PadA13)
- CPU0 pad A14: (no net) -> Net-(CPU0-PadA14)
- CPU0 pad A15: (no net) -> Net-(CPU0-PadA15)
- CPU0 pad A16: (no net) -> Net-(CPU0-PadA16)
- CPU0 pad A17: (no net) -> Net-(CPU0-PadA17)
- CPU0 pad A18: (no net) -> Net-(CPU0-PadA18)
- CPU0 pad A2: (no net) -> Net-(CPU0-PadA2)
- CPU0 pad A20: (no net) -> Net-(CPU0-PadA20)
- CPU0 pad A21: (no net) -> Net-(CPU0-PadA21)
- CPU0 pad A3: (no net) -> Net-(CPU0-PadA3)
- CPU0 pad A4: (no net) -> Net-(CPU0-PadA4)
- CPU0 pad A5: (no net) -> Net-(CPU0-PadA5)
- CPU0 pad A6: (no net) -> Net-(CPU0-PadA6)
- CPU0 pad A7: (no net) -> Net-(CPU0-PadA7)
- CPU0 pad A8: (no net) -> Net-(CPU0-PadA8)
- CPU0 pad A9: (no net) -> Net-(CPU0-PadA9)
- CPU0 pad B1: (no net) -> Net-(CPU0-PadB1)
- CPU0 pad B10: (no net) -> Net-(CPU0-PadB10)
- CPU0 pad B11: (no net) -> Net-(CPU0-PadB11)
- CPU0 pad B12: (no net) -> Net-(CPU0-PadB12)
- CPU0 pad B14: (no net) -> Net-(CPU0-PadB14)
- CPU0 pad B15: (no net) -> Net-(CPU0-PadB15)
- CPU0 pad B16: (no net) -> Net-(CPU0-PadB16)
- CPU0 pad B18: (no net) -> Net-(CPU0-PadB18)
- CPU0 pad B19: (no net) -> Net-(CPU0-PadB19)
- CPU0 pad B2: (no net) -> Net-(CPU0-PadB2)
- CPU0 pad B20: (no net) -> Net-(CPU0-PadB20)
- CPU0 pad B21: (no net) -> Net-(CPU0-PadB21)
- CPU0 pad B22: (no net) -> Net-(CPU0-PadB22)
- CPU0 pad B3: (no net) -> Net-(CPU0-PadB3)
- CPU0 pad B4: (no net) -> Net-(CPU0-PadB4)
- CPU0 pad B6: (no net) -> Net-(CPU0-PadB6)
- CPU0 pad B7: (no net) -> Net-(CPU0-PadB7)
- CPU0 pad B8: (no net) -> Net-(CPU0-PadB8)
- CPU0 pad C1: (no net) -> Net-(CPU0-PadC1)
- CPU0 pad C10: (no net) -> Net-(CPU0-PadC10)
- CPU0 pad C11: (no net) -> Net-(CPU0-PadC11)
- CPU0 pad C12: (no net) -> Net-(CPU0-PadC12)
- CPU0 pad C13: (no net) -> Net-(CPU0-PadC13)
- CPU0 pad C14: (no net) -> Net-(CPU0-PadC14)
- CPU0 pad C15: (no net) -> Net-(CPU0-PadC15)
- CPU0 pad C16: (no net) -> Net-(CPU0-PadC16)
- CPU0 pad C17: (no net) -> Net-(CPU0-PadC17)
- CPU0 pad C19: (no net) -> Net-(CPU0-PadC19)
- CPU0 pad C2: (no net) -> P1V5_BRIDGE
- CPU0 pad C20: (no net) -> Net-(CPU0-PadC20)
- CPU0 pad C21: (no net) -> P3V3_CPU
- CPU0 pad C22: (no net) -> Net-(CPU0-PadC22)
- CPU0 pad C3: (no net) -> Net-(CPU0-PadC3)
- CPU0 pad C5: (no net) -> Net-(CPU0-PadC5)
- CPU0 pad C6: (no net) -> Net-(CPU0-PadC6)
- CPU0 pad C7: (no net) -> Net-(CPU0-PadC7)
- CPU0 pad C8: (no net) -> Net-(CPU0-PadC8)
- CPU0 pad C9: (no net) -> Net-(CPU0-PadC9)
- CPU0 pad D1: (no net) -> Net-(CPU0-PadD1)
- CPU0 pad D10: (no net) -> Net-(CPU0-PadD10)
- CPU0 pad D11: (no net) -> Net-(CPU0-PadD11)
- CPU0 pad D12: (no net) -> Net-(CPU0-PadD12)
- CPU0 pad D13: (no net) -> Net-(CPU0-PadD13)
- CPU0 pad D14: (no net) -> Net-(CPU0-PadD14)
- CPU0 pad D15: (no net) -> Net-(CPU0-PadD15)
- CPU0 pad D17: (no net) -> Net-(CPU0-PadD17)
- CPU0 pad D19: (no net) -> Net-(CPU0-PadD19)
- CPU0 pad D2: (no net) -> Net-(CPU0-PadD2)
- CPU0 pad D20: (no net) -> Net-(CPU0-PadD20)
- CPU0 pad D21: (no net) -> /CPU0/CACHE_~UB
- CPU0 pad D22: (no net) -> /CPU0/CACHE_~LB
- CPU0 pad D6: (no net) -> Net-(CPU0-PadD6)
- CPU0 pad D7: (no net) -> Net-(CPU0-PadD7)
- CPU0 pad D8: (no net) -> Net-(CPU0-PadD8)
- CPU0 pad D9: (no net) -> Net-(CPU0-PadD9)
- CPU0 pad E1: (no net) -> Net-(CPU0-PadE1)
- CPU0 pad E12: (no net) -> Net-(CPU0-PadE12)
- CPU0 pad E13: (no net) -> Net-(CPU0-PadE13)
- CPU0 pad E14: (no net) -> Net-(CPU0-PadE14)
- CPU0 pad E16: (no net) -> Net-(CPU0-PadE16)
- CPU0 pad E17: (no net) -> Net-(CPU0-PadE17)
- CPU0 pad E19: (no net) -> P3V3_CPU
- CPU0 pad E20: (no net) -> /CPU0/CACHE_DQ15
- CPU0 pad E22: (no net) -> /CPU0/CACHE_DQ14
- CPU0 pad E3: (no net) -> Net-(CPU0-PadE3)
- CPU0 pad E9: (no net) -> Net-(CPU0-PadE9)
- CPU0 pad F1: (no net) -> Net-(CPU0-PadF1)
- CPU0 pad F12: (no net) -> Net-(CPU0-PadF12)
- CPU0 pad F13: (no net) -> Net-(CPU0-PadF13)
- CPU0 pad F14: (no net) -> Net-(CPU0-PadF14)
- CPU0 pad F15: (no net) -> Net-(CPU0-PadF15)
- CPU0 pad F18: (no net) -> Net-(CPU0-PadF18)
- CPU0 pad F19: (no net) -> Net-(CPU0-PadF19)
- CPU0 pad F2: (no net) -> Net-(CPU0-PadF2)
- CPU0 pad F20: (no net) -> /CPU0/CACHE_~OE
- CPU0 pad F21: (no net) -> /CPU0/CACHE_DQ13
- CPU0 pad F22: (no net) -> /CPU0/CACHE_DQ12
- CPU0 pad F3: (no net) -> Net-(CPU0-PadF3)
- CPU0 pad F4: (no net) -> P1V5_BRIDGE
- CPU0 pad F5: (no net) -> Net-(CPU0-PadF5)
- CPU0 pad F6: (no net) -> P1V5_BRIDGE
- CPU0 pad G1: (no net) -> Net-(CPU0-PadG1)
- CPU0 pad G10: (no net) -> Net-(CPU0-PadG10)
- CPU0 pad G13: (no net) -> Net-(CPU0-PadG13)
- CPU0 pad G14: (no net) -> Net-(CPU0-PadG14)
- CPU0 pad G19: (no net) -> /CPU0/CACHE_A7
- CPU0 pad G2: (no net) -> P1V5_BRIDGE
- CPU0 pad G20: (no net) -> /CPU0/CACHE_DQ11
- CPU0 pad G21: (no net) -> P3V3_CPU
- CPU0 pad G22: (no net) -> /CPU0/CACHE_DQ10
- CPU0 pad G3: (no net) -> Net-(CPU0-PadG3)
- CPU0 pad G4: (no net) -> /CPU0/BUSREQ#
- CPU0 pad G6: (no net) -> Net-(CPU0-PadG6)
- CPU0 pad H1: (no net) -> /Multibridge/CPU_D30
- CPU0 pad H12: (no net) -> Net-(CPU0-PadH12)
- CPU0 pad H13: (no net) -> Net-(CPU0-PadH13)
- CPU0 pad H14: (no net) -> Net-(CPU0-PadH14)
- CPU0 pad H18: (no net) -> Net-(CPU0-PadH18)
- CPU0 pad H19: (no net) -> /CPU0/CACHE_A6
- CPU0 pad H2: (no net) -> /CPU0/BUSINT#
- CPU0 pad H20: (no net) -> Net-(CPU0-PadH20)
- CPU0 pad H21: (no net) -> /CPU0/CACHE_DQ9
- CPU0 pad H22: (no net) -> /CPU0/CACHE_DQ8
- CPU0 pad H3: (no net) -> /Multibridge/CPU_WR#
- CPU0 pad H4: (no net) -> /CPU0/ADDR#
- CPU0 pad H5: (no net) -> Net-(CPU0-PadH5)
- CPU0 pad H6: (no net) -> Net-(CPU0-PadH6)
- CPU0 pad H8: (no net) -> Net-(CPU0-PadH8)
- CPU0 pad J1: (no net) -> /CPU0/BUSACK#
- CPU0 pad J17: (no net) -> Net-(CPU0-PadJ17)
- CPU0 pad J18: (no net) -> P3V3_CPU
- CPU0 pad J19: (no net) -> /CPU0/CACHE_A5
- CPU0 pad J20: (no net) -> /CPU0/CACHE_A8
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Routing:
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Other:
- net class Default: clearance 0.1016 -> 0.125; trace_width 0.1016 -> 0.125
- rule trace_clearance: 0.1016 -> 0.125
